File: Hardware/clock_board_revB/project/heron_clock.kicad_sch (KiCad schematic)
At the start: 110 parts, among them J1 5V_IN, J10 PPS_B200_2, J2 PPS_IN, J3 REF_B210_1, J4 REF_B210_2, J5 REF_B200_1, J6 REF_B200_2, J7 PPS_B210_1, J8 PPS_B210_2, J9 PPS_B200_1, U1 LP5907MFX-3.3/NOPB, U2 TLV75533PDBVR, U3 SiT5155AI-FK-33E0-10.000000, U4 LMK1C1104PWR, U5 SN74LVC1G17DBVR, U6 SN74LVC125APWR

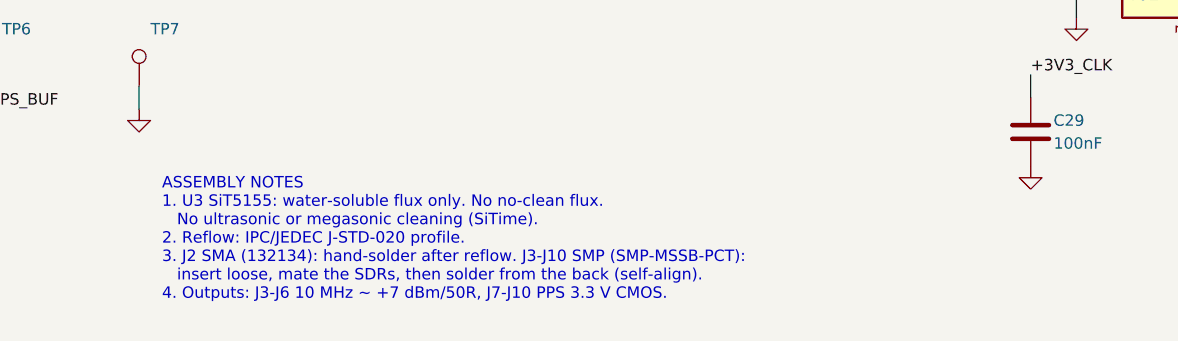
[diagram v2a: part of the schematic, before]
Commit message: Change clock board SMP jacks to SMP-MSSB-PCT10T and L1-L8 to Abracon
J3-J10 change from Amphenol SMP-MSSB-PCT ($29) to SMP-MSSB-PCT10T
($6.89). The legs stay through-hole in +/-0.2 mm float holes. The
signal contact is now a surface-mount tab, so the footprint gets a
tab pad (no paste) and the copper keep-out from the Amphenol drawing.
All jacks have the tab toward +x. The 10 MHz traces end on the tab.
The PPS jacks get a dog-leg to the ESD diode; J9 goes through two
vias on B.Cu because PPS4_Y passes next to it.

L1-L8 change from Coilcraft 0805CS-821XJRC (Digi-Key Marketplace
only) to Abracon AISC-0805-R82J-T (same size, core and specs).

DRC: 0 errors, 0 unconnected pads, 0 parity issues. Courtyard
overlaps at the 10 MHz jack tab side and starved thermals on some
leg pads remain as warnings (see the README).

Co-Authored-By: Claude Opus 5.5 <noreply@anthropic.com>
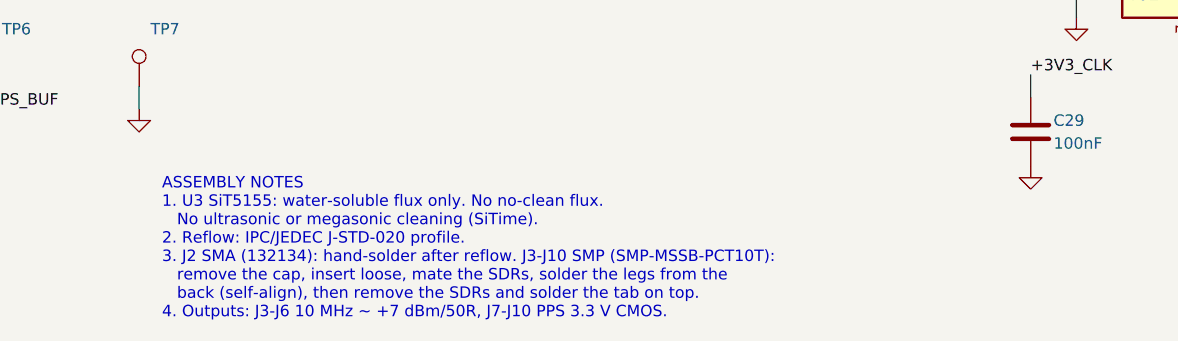
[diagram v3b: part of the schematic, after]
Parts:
- J10, J3, J4, J5, J6, J7, J8, J9: footprint HERON_Clock:SMP_Amphenol_SMP-MSSB-PCT_Vertical_Float -> HERON_Clock:SMP_Amphenol_SMP-MSSB-PCT10T_Vertical_Float; MPN SMP-MSSB-PCT -> SMP-MSSB-PCT10T
- L1, L2, L3, L4, L5, L6, L7, L8: MPN 0805CS-821XJRC -> AISC-0805-R82J-T; Manufacturer Coilcraft -> Abracon
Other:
- note added: "ASSEMBLY NOTES 1. U3 SiT5155: water-soluble flux only. No no-clean flux. No ultrasonic or megasonic cleaning (SiTime). 2. Reflow: IPC/JEDEC J-STD-020 profile. 3. J2 SMA (132134): hand-solder after reflow. J3-J10 SMP (SMP-MSSB-PCT10T): remove the cap, insert loose, mate the SDRs, solder the legs from the back (self-align), then remove the SDRs and solder the tab on top. 4. Outputs: J3-J6 10 MHz ~ 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"
- note removed: "ASSEMBLY NOTES 1. U3 SiT5155: water-soluble flux only. No no-clean flux. No ultrasonic or megasonic cleaning (SiTime). 2. Reflow: IPC/JEDEC J-STD-020 profile. 3. J2 SMA (132134): hand-solder after reflow. J3-J10 SMP (SMP-MSSB-PCT): insert loose, mate the SDRs, then solder from the back (self-align). 4. Outputs: J3-J6 10 MHz ~ +7 dBm/50R, J7-J10 PPS 3.3 V CMOS."
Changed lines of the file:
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@@
         (font
           (size 1.27 1.27)) hide))
-    (property "Manufacturer" "Coilcraft"
+    (property "Manufacturer" "Abracon"
       (at 242.57 35.56 90)
       (effects
         (font
           (size 1.27 1.27)) hide))
-    (property "MPN" "0805CS-821XJRC"
+    (property "MPN" "AISC-0805-R82J-T"
       (at 242.57 35.56 90)
       (effects
@@
         (font
           (size 1.27 1.27)) hide))
-    (property "Manufacturer" "Coilcraft"
+    (property "Manufacturer" "Abracon"
       (at 262.89 35.56 90)
       (effects
         (font
           (size 1.27 1.27)) hide))
-    (property "MPN" "0805CS-821XJRC"
+    (property "MPN" "AISC-0805-R82J-T"
       (at 262.89 35.56 90)
       (effects
@@
         (font
           (size 1.27 1.27))))
-    (property "Footprint" "HERON_Clock:SMP_Amphenol_SMP-MSSB-PCT_Vertical_Float"
+    (property "Footprint" "HERON_Clock:SMP_Amphenol_SMP-MSSB-PCT10T_Vertical_Float"
       (at 332.74 35.56 0)
       (effects
@@
         (font
           (size 1.27 1.27)) hide))
-    (property "MPN" "SMP-MSSB-PCT"
+    (property "MPN" "SMP-MSSB-PCT10T"
       (at 332.74 35.56 0)
       (effects
@@
         (font
           (size 1.27 1.27)) hide))
-    (property "Manufacturer" "Coilcraft"
+    (property "Manufacturer" "Abracon"
       (at 242.57 63.5 90)
       (effects
         (font
           (size 1.27 1.27)) hide))
-    (property "MPN" "0805CS-821XJRC"
+    (property "MPN" "AISC-0805-R82J-T"
       (at 242.57 63.5 90)
       (effects
@@
         (font
           (size 1.27 1.27)) hide))
-    (property "Manufacturer" "Coilcraft"
+    (property "Manufacturer" "Abracon"
       (at 262.89 63.5 90)
       (effects
         (font
           (size 1.27 1.27)) hide))
-    (property "MPN" "0805CS-821XJRC"
+    (property "MPN" "AISC-0805-R82J-T"
       (at 262.89 63.5 90)
       (effects
@@
         (font
           (size 1.27 1.27))))
-    (property "Footprint" "HERON_Clock:SMP_Amphenol_SMP-MSSB-PCT_Vertical_Float"
+    (property "Footprint" "HERON_Clock:SMP_Amphenol_SMP-MSSB-PCT10T_Vertical_Float"
       (at 332.74 63.5 0)
       (effects
@@
         (font
           (size 1.27 1.27)) hide))
-    (property "MPN" "SMP-MSSB-PCT"
+    (property "MPN" "SMP-MSSB-PCT10T"
       (at 332.74 63.5 0)
       (effects
@@
         (font
           (size 1.27 1.27)) hide))
-    (property "Manufacturer" "Coilcraft"
+    (property "Manufacturer" "Abracon"
       (at 242.57 91.44 90)
       (effects
         (font
           (size 1.27 1.27)) hide))
-    (property "MPN" "0805CS-821XJRC"
+    (property "MPN" "AISC-0805-R82J-T"
       (at 242.57 91.44 90)
       (effects
@@
         (font
           (size 1.27 1.27)) hide))
-    (property "Manufacturer" "Coilcraft"
+    (property "Manufacturer" "Abracon"
       (at 262.89 91.44 90)
       (effects
         (font
           (size 1.27 1.27)) hide))
-    (property "MPN" "0805CS-821XJRC"
+    (property "MPN" "AISC-0805-R82J-T"
       (at 262.89 91.44 90)
       (effects
@@
         (font
           (size 1.27 1.27))))
-    (property "Footprint" "HERON_Clock:SMP_Amphenol_SMP-MSSB-PCT_Vertical_Float"
+    (property "Footprint" "HERON_Clock:SMP_Amphenol_SMP-MSSB-PCT10T_Vertical_Float"
       (at 332.74 91.44 0)
       (effects
@@
         (font
           (size 1.27 1.27)) hide))
-    (property "MPN" "SMP-MSSB-PCT"
+    (property "MPN" "SMP-MSSB-PCT10T"
       (at 332.74 91.44 0)
       (effects
@@
         (font
           (size 1.27 1.27)) hide))
-    (property "Manufacturer" "Coilcraft"
+    (property "Manufacturer" "Abracon"
       (at 242.57 119.38 90)
       (effects
         (font
           (size 1.27 1.27)) hide))
-    (property "MPN" "0805CS-821XJRC"
+    (property "MPN" "AISC-0805-R82J-T"
       (at 242.57 119.38 90)
       (effects
@@
         (font
           (size 1.27 1.27)) hide))
-    (property "Manufacturer" "Coilcraft"
+    (property "Manufacturer" "Abracon"
       (at 262.89 119.38 90)
       (effects
         (font
           (size 1.27 1.27)) hide))
-    (property "MPN" "0805CS-821XJRC"
+    (property "MPN" "AISC-0805-R82J-T"
       (at 262.89 119.38 90)
       (effects
@@
         (font
           (size 1.27 1.27))))
-    (property "Footprint" "HERON_Clock:SMP_Amphenol_SMP-MSSB-PCT_Vertical_Float"
+    (property "Footprint" "HERON_Clock:SMP_Amphenol_SMP-MSSB-PCT10T_Vertical_Float"
       (at 332.74 119.38 0)
       (effects
@@
         (font
           (size 1.27 1.27)) hide))
-    (property "MPN" "SMP-MSSB-PCT"
+    (property "MPN" "SMP-MSSB-PCT10T"
       (at 332.74 119.38 0)
       (effects
@@
         (font
           (size 1.27 1.27))))
-    (property "Footprint" "HERON_Clock:SMP_Amphenol_SMP-MSSB-PCT_Vertical_Float"
+    (property "Footprint" "HERON_Clock:SMP_Amphenol_SMP-MSSB-PCT10T_Vertical_Float"
       (at 309.88 190.5 0)
       (effects
@@
         (font
           (size 1.27 1.27)) hide))
-    (property "MPN" "SMP-MSSB-PCT"
+    (property "MPN" "SMP-MSSB-PCT10T"
       (at 309.88 190.5 0)
       (effects
@@
         (font
           (size 1.27 1.27))))
-    (property "Footprint" "HERON_Clock:SMP_Amphenol_SMP-MSSB-PCT_Vertical_Float"
+    (property "Footprint" "HERON_Clock:SMP_Amphenol_SMP-MSSB-PCT10T_Vertical_Float"
       (at 309.88 208.28 0)
       (effects
@@
         (font
           (size 1.27 1.27)) hide))
-    (property "MPN" "SMP-MSSB-PCT"
+    (property "MPN" "SMP-MSSB-PCT10T"
       (at 309.88 208.28 0)
       (effects
@@
         (font
           (size 1.27 1.27))))
-    (property "Footprint" "HERON_Clock:SMP_Amphenol_SMP-MSSB-PCT_Vertical_Float"
+    (property "Footprint" "HERON_Clock:SMP_Amphenol_SMP-MSSB-PCT10T_Vertical_Float"
       (at 309.88 226.06 0)
       (effects
@@
         (font
           (size 1.27 1.27)) hide))
-    (property "MPN" "SMP-MSSB-PCT"
+    (property "MPN" "SMP-MSSB-PCT10T"
       (at 309.88 226.06 0)
       (effects
@@
         (font
           (size 1.27 1.27))))
-    (property "Footprint" "HERON_Clock:SMP_Amphenol_SMP-MSSB-PCT_Vertical_Float"
+    (property "Footprint" "HERON_Clock:SMP_Amphenol_SMP-MSSB-PCT10T_Vertical_Float"
       (at 309.88 243.84 0)
       (effects
@@
         (font
           (size 1.27 1.27)) hide))
-    (property "MPN" "SMP-MSSB-PCT"
+    (property "MPN" "SMP-MSSB-PCT10T"
       (at 309.88 243.84 0)
       (effects
@@
           (reference "FID3")
           (unit 1)))))
-  (text "ASSEMBLY NOTES\n1. U3 SiT5155: water-soluble flux only. No no-clean flux.\n   No ultrasonic or megasonic cleaning (SiTime).\n2. Reflow: IPC/JEDEC J-STD-020 profile.\n3. J2 SMA (132134): hand-solder after reflow. J3-J10 SMP (SMP-MSSB-PCT):\n   insert loose, mate the SDRs, then solder from the back (self-align).\n4. Outputs: J3-J6 10 MHz ~ +7 dBm/50R, J7-J10 PPS 3.3 V CMOS."
+  (text "ASSEMBLY NOTES\n1. U3 SiT5155: water-soluble flux only. No no-clean flux.\n   No ultrasonic or megasonic cleaning (SiTime).\n2. Reflow: IPC/JEDEC J-STD-020 profile.\n3. J2 SMA (132134): hand-solder after reflow. J3-J10 SMP (SMP-MSSB-PCT10T):\n   remove the cap, insert loose, mate the SDRs, solder the legs from the\n   back (self-align), then remove the SDRs and solder the tab on top.\n4. Outputs: J3-J6 10 MHz ~ +7 dBm/50R, J7-J10 PPS 3.3 V CMOS."
     (at 127 246.38 0)
     (effects
